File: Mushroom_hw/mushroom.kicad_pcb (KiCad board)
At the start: 2 copper layers, 49.2 x 83.8 mm, 129 parts, among them Q1 LED_RGB_WS2812B, Q2 LED_RGB, Q3 LED_RGB_WS2812B, Q4 LED_RGB, Q5 LED_RGB, Q6 LED_RGB_WS2812B, SW1 SWITCH_H

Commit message: + Component placement done
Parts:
- removed B1, B2, B3: BAT, BAT_AA
- removed C29, C30, C31: 0.1u, CAP_0603
- removed D1, D2, D3: SS14, DIODE_SMA_DO214AC
- removed DA3, DA4: TPS61042, DRB8
- removed F10, F11, F12, F13, F14, F15, F16, F17, F18, F19, F2, F20, F3, F4, F5, F6, F7, F8, F9: FUSE0R, SMD0603_FUSE
- removed L3: 6.8uH, IND_1210
- removed R10, R9: 390k, RES_0603
- removed R11, R16: 10k, RES_0603
- removed R12, R17: 13R, RES_0603
- removed R13, R18: 120k, RES_0603
- removed R14: 56k, RES_0603
- removed R15: 100k, RES_0603
- removed R19, R20, R21: 51R, RES_0603
- removed TP3: TESTPOINT, TESTPOINT_1MM
- removed XL14, XL16, XL17, XL18, XL20, XL21, XL22, XL24: CONN_3, SIL-3
- removed XL15, XL19, XL23: CONN_1, SIL1_ROUND_1MM8
- added BLN1: BALUN868JOHANSON, Radio:BALUN_JOHANSON868, F.Cu at (219.6, 130.0)
- added HOLE5: HOLE_METALLED, PCB:Hole2d4_out4d5mm, F.Cu at (249.0, 194.0)
- added HOLE6: HOLE_METALLED, PCB:Hole2d4_out4d5mm, F.Cu at (249.0, 124.0)
- added Logo1: Logo, Pictures:Ostranna_12d7_10d1, F.Cu at (239.0, 121.0)
- added RP3: REFPOINT, PCB:REF_POINT_1MM, B.Cu at (210.8, 195.2)
- added RP4: REFPOINT, PCB:REF_POINT_1MM, B.Cu at (250.2, 113.8)
- added SW2: BUTTON, BtnsSwitches:BTN_6x6_4x4, B.Cu at (243.0, 191.5)
- added SW3: BUTTON, BtnsSwitches:BTN_6x6_4x4, B.Cu at (221.5, 191.5)
- added SW4: BUTTON, BtnsSwitches:BTN_6x6_4x4, B.Cu at (232.0, 191.5)
- ANT1: value ANT_PCB_NOCNTR -> ANT_PCB_MONO; footprint ANT_FOLDED_DIPOLE2 -> Radio:ANT_868_ARMLETG
- C1, C20: value 0.1u -> 10u; footprint CAP_0603 -> Capacitors:CAP_0603
- C10: value 1u -> 10u; footprint CAP_0603 -> Capacitors:CAP_0603
- C11: value 10u -> 10n; footprint CAP_0805 -> Capacitors:CAP_0603
- C12, C23, C5, C7, C9: footprint CAP_0603 -> Capacitors:CAP_0603
- C13: value 10u -> 1u; footprint CAP_0805 -> Capacitors:CAP_0603
- C14: value 0.1u -> 220pF; footprint CAP_0603 -> Capacitors:CAP_0603
- C15, C21, C28, C3, C8: value 10u -> 0.1u; footprint CAP_0805 -> Capacitors:CAP_0603
- C16: footprint CAP_0805 -> Capacitors:CAP_0603
- C17: value 10pF -> 18pF; footprint CAP_0603 -> Capacitors:CAP_0603
- C18: value 10pF -> 10u; footprint CAP_0603 -> Capacitors:CAP_0603
- C19: value 0.1u -> 18pF; footprint CAP_0603 -> Capacitors:CAP_0603
- C2: value 10u -> 220pF; footprint CAP_0805 -> Capacitors:CAP_0603
- C22, C25, C27: value 220pF -> 0.1u; footprint CAP_0603 -> Capacitors:CAP_0603
- C24, C26: value 0.1u -> *; footprint CAP_0603 -> Capacitors:CAP_0402
- C4: value 0.1u -> 10n; footprint CAP_0603 -> Capacitors:CAP_0603
- C6: value 0.1u -> 3.3pF; footprint CAP_0603 -> Capacitors:CAP_0603
- DA1: value TPS61042 -> NCP583SQ; footprint DRB8 -> SOT:SC82AB
- DA2: value NCP583SQ -> MC74VHC1; footprint SC82AB -> SOT:SOT23-5
- DD1: value STM32L151CXTX -> STM32L151CxTx; footprint LQFP48 -> LQFP_TQFP:LQFP48
- DD2: value CC2500 -> CC1101; footprint QFN20 -> QFN_DFN:QFN20
- F1: value FUSE0R -> Fuse0R; footprint SMD0603_FUSE -> Resistors:RES_0603_FUSE
- HOLE1, HOLE2, HOLE3, HOLE4: footprint Hole3_5_out6mm -> PCB:Hole2d4_out4d5mm
- L1: value 6.8uH -> BLM15AG102SN1; footprint IND_1210 -> Inductors:IND_0402
- L2: value 6.8uH -> *; footprint IND_1210 -> Inductors:IND_0402
- Q1: value LED_RGB_WS2812B -> 2N7002; footprint LED_WS2812B -> SOT:SOT23-3
- Q2: value LED_RGB -> IRLML9303; footprint LED_HH5050_RGB -> SOT:SOT23-3
- Q3: value LED_RGB_WS2812B -> ALS-PT19-315C; footprint LED_WS2812B -> Resistors:RES_0603
- Q4, Q5: value LED_RGB -> LED_RGB_WS2812B; footprint LED_HH5050_RGB -> LEDs:LED_WS2812B
- Q6: footprint LED_WS2812B -> LEDs:LED_WS2812B
- R1, R2: value 4K7 -> 100k; footprint RES_0603 -> Resistors:RES_0603
- R3: footprint RES_0603 -> Resistors:RES_0603
- R4: value 150 -> 100k; footprint RES_0603 -> Resistors:RES_0603
- R5: value 10k -> 20k; footprint RES_0603 -> Resistors:RES_0603
- R6: value 13R -> 56k; footprint RES_0603 -> Resistors:RES_0603
- R7: value 120k -> 10k; footprint RES_0603 -> Resistors:RES_0603
- R8: value 100k -> 10k; footprint RES_0603 -> Resistors:RES_0603
- RP1, RP2: footprint REF_POINT_1MM -> PCB:REF_POINT_1MM
- SW1: value SWITCH_H -> SWITCH; footprint SWITCH_SS9 -> BtnsSwitches:SW_SS-1P2T
- TP1, TP2: footprint TESTPOINT_1MM -> PCB:TESTPOINT_1MM
- XL1: value CONN_3 -> CONN_6; footprint SIL-3 -> Connectors:PLS-6; moved to B.Cu
- XL10, XL12, XL6, XL8: footprint SIL-3 -> Connectors:PLS-3
- XL11, XL7: footprint SIL1_ROUND_1MM8 -> Connectors:SIL1_ROUND_1MM8
- XL13, XL5, XL9: value CONN_3 -> CONN_1; footprint SIL-3 -> Connectors:SIL1_ROUND_1MM8
- XL2: value ST_SWD -> CONN_1; footprint SIL-4 -> Connectors:PLS-1Rnd
- XL3: value CONN_4 -> CONN_2; footprint SIL-4 -> Connectors:W02_Pitch_2d54; moved to B.Cu
- XL4: value CONN_4 -> CONN_3; footprint SIL-4 -> Connectors:PLS-3
- XTAL1: footprint CRYSTAL_03225C4 -> Quartz:03225C4
- moved RP1 103.6 mm to (250.2, 113.8)
- moved XL2 86.2 mm to (250.5, 128.5)
- moved C9 71.9 mm to (223.8, 134.7)
- moved C6 71.0 mm to (222.5, 130.2), turned to 0 degrees
- moved C4 64.7 mm to (217.5, 129.5)
- moved C12 62.2 mm to (219.5, 139.9)
- moved RP2 59.6 mm to (210.8, 195.2)
- moved C21 56.6 mm to (221.1, 139.9), turned to 90 degrees
- moved L2 54.3 mm to (219.0, 127.8), turned to 270 degrees
- moved HOLE2 54.1 mm to (220.0, 165.0)
- moved DA2 48.9 mm to (211.8, 155.1), turned to 0 degrees
- moved R2 48.8 mm to (212.9, 165.2)
- moved C14 48.6 mm to (214.0, 135.5)
- moved C28 48.6 mm to (233.4, 157.0)
- moved HOLE4 47.4 mm to (207.0, 124.0)
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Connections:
- ANT1 pad 1: /Ant -> /ANT2
- C1 pad 1: +BATT -> GND
- C1 pad 2: GND -> +3.3V
- C10 pad 1: +3.3V -> +BATT
- C11 pad 1: /RED_P -> +3.3V
- C12 pad 1: +3.3V -> VCC
- C14 pad 1: +BATT -> VCC
- C15 pad 1: +BATT -> +3.3V
- C16 pad 1: /GREEN_P -> +3.3V
- C18 pad 1: N-000005 -> GND
- C18 pad 2: GND -> PwrUnst
- C19 pad 1: N-0000010 -> Net-(C19-Pad1)
- C2 pad 1: +BATT -> VCC
- C20 pad 1: +BATT -> GND
- C20 pad 2: GND -> PwrUnst
- C21 pad 1: +BATT -> GND
- C21 pad 2: GND -> Net-(C21-Pad2)
- C22 pad 1: +3.3V -> PwrUnst
- C23 pad 1: +3.3V -> /ADC_LUM
- C24 pad 1: +3.3V -> /ANT1
- C25 pad 1: +3.3V -> PwrUnst
- C26 pad 1: +3.3V -> /ANT2
- C27 pad 1: +3.3V -> PwrUnst
- C28 pad 1: /BLUE_P -> PwrUnst
- C4 pad 1: +3.3V -> VCC
- C6 pad 1: +BATT -> VCC
- C7 pad 1: +3.3V -> +BATT
- C8 pad 1: +BATT -> +3.3V
- C9 pad 1: +3.3V -> VCC
- DA1 pad 1: /RED_N -> +BATT
- DA1 pad 2: N-000007 -> GND
- DA1 pad 3: +BATT -> +3.3V
- DA1 pad 4: N-000006 -> +BATT
- DA2 pad 1: +BATT -> Net-(DA2-Pad1)
- DA2 pad 2: GND -> /WS_CTRL
- DA2 pad 3: +3.3V -> GND
- DA2 pad 4: +BATT -> /DIN0
- DD1 pad 10: N-000008 -> /BTN1
- DD1 pad 11: /CC_GDO2 -> /BTN2
- DD1 pad 12: /CC_CS -> /ADC_BATTERY
- DD1 pad 14: /BRIGHTNESS -> /CC_CS
- DD1 pad 18: /RED_PWM -> /ADC_LUM
- DD1 pad 19: /GREEN_PWM -> /MEAS_LUM
- DD1 pad 21: N-0000032 -> (no net)
- DD1 pad 22: N-0000033 -> (no net)
- DD1 pad 25: N-0000031 -> (no net)
- DD1 pad 27: (no net) -> /PWR_EN
- DD1 pad 28: /DIN0 -> /WS_CTRL
- DD1 pad 29: (no net) -> /BTN3
- DD1 pad 41: /BLUE_PWM -> (no net)
- DD1 pad 43: /PeriphPwr -> /NO_RADIO
- DD1 pad 45: /P_SCL -> (no net)
- DD1 pad 46: /P_SDA -> (no net)
- DD2 pad 10: N-000005 -> Net-(C19-Pad1)
- DD2 pad 11: +3.3V -> VCC
- DD2 pad 12: /Ant -> /RF1
- DD2 pad 13: /Ant -> /RF2
- DD2 pad 14: +3.3V -> VCC
- DD2 pad 15: +3.3V -> VCC
- DD2 pad 17: N-0000013 -> Net-(DD2-Pad17)
- DD2 pad 18: +3.3V -> VCC
- DD2 pad 3: /CC_GDO2 -> (no net)
- DD2 pad 4: +3.3V -> VCC
- DD2 pad 5: N-0000010 -> Net-(C21-Pad2)
- DD2 pad 9: +3.3V -> VCC
- F1 pad 1: GND -> +3.3V
- F1 pad 2: N-0000070 -> /NO_RADIO
- L1 pad 1: N-0000017 -> VCC
- L1 pad 2: +BATT -> +3.3V
- L2 pad 1: N-0000016 -> /ANT2
- L2 pad 2: +BATT -> /ANT1
- Q1 pad 1: +BATT -> /PWR_EN
- Q1 pad 2: N-0000059 -> GND
- Q1 pad 3: GND -> Net-(Q1-Pad3)
- Q3 pad 1: +BATT -> +3.3V
- Q3 pad 2: N-0000058 -> /ADC_LUM
- Q6 pad 1: +BATT -> PwrUnst
- Q6 pad 4: N-0000058 -> Net-(Q5-Pad2)
- R1 pad 1: /P_SCL -> PwrUnst
- R1 pad 2: /PeriphPwr -> /ADC_BATTERY
- R2 pad 1: /P_SDA -> /ADC_BATTERY
- R2 pad 2: /PeriphPwr -> GND
- R3 pad 1: /RED_PWM -> /PWR_EN
- R4 pad 1: /PeriphPwr1 -> +BATT
- R4 pad 2: /PeriphPwr -> Net-(Q1-Pad3)
- R5 pad 1: N-000007 -> /CC_CS
- R5 pad 2: N-000006 -> VCC
- R6 pad 1: N-000007 -> Net-(DD2-Pad17)
- R7 pad 1: N-000006 -> Net-(DA2-Pad1)
- R7 pad 2: /BRIGHTNESS -> PwrUnst
- R8 pad 1: /GREEN_PWM -> /ADC_LUM
- R8 pad 2: GND -> /MEAS_LUM
- SW1 pad 1: /BAT_IN -> +BATT
- SW1 pad 2: +BATT -> /BAT_IN
- XL1 pad 1: GND -> +3.3V
- XL1 pad 2: /UART_TX -> /SWCLK
- XL1 pad 3: /UART_RX -> GND
- XL10 pad 1: /DIN1 -> /DIN3
- XL10 pad 2: +BATT -> PwrUnst
- XL10 pad 3: /DIN2 -> /DIN4
- XL11 pad 1: N-0000071 -> GND
- XL12 pad 1: N-0000022 -> /DIN4
- XL12 pad 2: N-0000021 -> PwrUnst
- XL12 pad 3: N-0000020 -> (no net)
- XL13 pad 1: N-0000022 -> GND
- XL2 pad 1: +3.3V -> GND
- XL3 pad 1: /PeriphPwr1 -> /BAT_IN
- XL3 pad 2: /P_SCL -> GND
- XL4 pad 1: N-0000032 -> /DIN0
- XL4 pad 2: N-0000033 -> PwrUnst
- XL4 pad 3: N-0000031 -> /DIN1
- XL5 pad 1: /RED_P -> GND
- XL6 pad 1: /DIN0 -> /DIN1
- XL6 pad 2: +BATT -> PwrUnst
- XL6 pad 3: /DIN1 -> /DIN2
- XL7 pad 1: N-0000070 -> GND
- XL8 pad 1: N-0000028 -> /DIN2
- XL8 pad 2: N-0000027 -> PwrUnst
- XL8 pad 3: N-0000026 -> /DIN3
- XL9 pad 1: N-0000028 -> GND
- XTAL1 pad 2: N-000005 -> Net-(C19-Pad1)
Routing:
- net GND: track 812.5 -> 0.00 mm, vias 151 -> 0
- net +3.3V: track 177.8 -> 0.00 mm, vias 10 -> 0
- net +BATT: track 159.2 -> 0.00 mm, vias 2 -> 0
- net /BLUE_P: track 78.3 -> 0.00 mm, vias 1 -> 0
- net /BRIGHTNESS: track 73.8 -> 0.00 mm, vias 4 -> 0
- net /BLUE_PWM: track 68.9 -> 0.00 mm, vias 2 -> 0
- net /GREEN_P: track 62.2 -> 0.00 mm, vias 1 -> 0
- net /GREEN_PWM: track 61.7 -> 0.00 mm, vias 2 -> 0
- net /RED_N: track 60.8 -> 0.00 mm, vias 3 -> 0
- net /RED_PWM: track 58.2 -> 0.00 mm, vias 2 -> 0
- net /BLUE_N: track 58.1 -> 0.00 mm, vias 4 -> 0
- net /CC_GDO2: track 58.0 -> 0.00 mm
- net /DIN0: track 57.0 -> 0.00 mm, vias 1 -> 0
- net /CC_MOSI: track 55.4 -> 0.00 mm
- net /CC_MISO: track 55.0 -> 0.00 mm
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- removed copper zone on B.Cu, net GND
- removed copper zone on F.Cu, net GND
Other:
- board size 49.2 x 83.8 mm -> 48 x 85 mm

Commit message: HW2 sent to production
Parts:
- moved XL10 11.5 mm to (236.6, 172.8)
- moved XL12 11.4 mm to (225.2, 172.8)
- moved R5 10.2 mm to (224.0, 139.8), turned to 270 degrees
- moved TP2 5.68 mm to (221.5, 142.4)
- moved L1 2.40 mm to (213.6, 138.6), turned to 180 degrees
- moved C17 1.02 mm to (226.4, 137.6)
- moved XTAL1 0.41 mm to (226.4, 134.4)
- moved C9 0.30 mm to (223.8, 134.4)
- moved C19 0.22 mm to (226.4, 131.2)
- moved C12 0.14 mm to (219.6, 139.8)
- moved C21 0.14 mm to (221.2, 139.8)
- moved C4 0.14 mm to (217.4, 129.4)
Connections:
- DD1 pad 11: /BTN2 -> /BTN3
- DD1 pad 29: /BTN3 -> /BTN2
- SW3 pad 1: /BTN2 -> /BTN3
- SW4 pad 1: /BTN3 -> /BTN2
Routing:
- net GND: track 0.00 -> 1013.3 mm, vias 0 -> 209
- net PwrUnst: track 0.00 -> 131.5 mm, vias 0 -> 2
- net +3.3V: track 0.00 -> 121.7 mm, vias 0 -> 6
- net VCC: track 0.00 -> 56.5 mm, vias 0 -> 6
- net /BTN2: track 0.00 -> 46.0 mm, vias 0 -> 1
- net /BTN1: track 0.00 -> 42.3 mm, vias 0 -> 1
- net /CC_CS: track 0.00 -> 38.7 mm, vias 0 -> 2
- net /CC_GDO0: track 0.00 -> 36.9 mm, vias 0 -> 2
- net /CC_MOSI: track 0.00 -> 35.7 mm, vias 0 -> 2
- net /CC_MISO: track 0.00 -> 34.8 mm, vias 0 -> 2
- net /CC_SCK: track 0.00 -> 34.7 mm, vias 0 -> 2
- net /UART_RX: track 0.00 -> 29.8 mm, vias 0 -> 1
- net /BTN3: track 0.00 -> 29.7 mm, vias 0 -> 1
- net /UART_TX: track 0.00 -> 27.8 mm, vias 0 -> 1
- net +BATT: track 0.00 -> 26.0 mm
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- added copper zone on B.Cu, net GND
- added copper zone on F.Cu, net GND
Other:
- net class Default: via_dia 0.9 -> 0.7; via_drill 0.4 -> 0.3
- net class Wide: via_dia 0.9 -> 0.7; via_drill 0.4 -> 0.3
- rule via_min_drill: 0.4 -> 0.2
- rule via_min_size: 0.889 -> 0.6
- board text added: "+"
- board text added: "-"
- board text added: "3V3 Power Supply"
- board text added: "Btn1"
- board text added: "Btn2"
- board text added: "Btn3"
- board text added: "Crystal Mushroom v2"
- board text added: "GND"
- board text added: "In"
- board text added: "LED A"
- board text added: "LED B"
- board text added: "LED C"
- board text added: "LED Power Control"
- board text added: "LED1"
- board text added: "LED2"
- board text added: "LED3"
- board text added: "LED4"
- board text added: "LED5"
- board text added: "Level Shifter"
- board text added: "Light detector"
- board text added: "MCU"
- board text added: "Ostranna"
- board text added: "Out"
- board text added: "Radio"
- board text added: "Solder if radio not mounted"

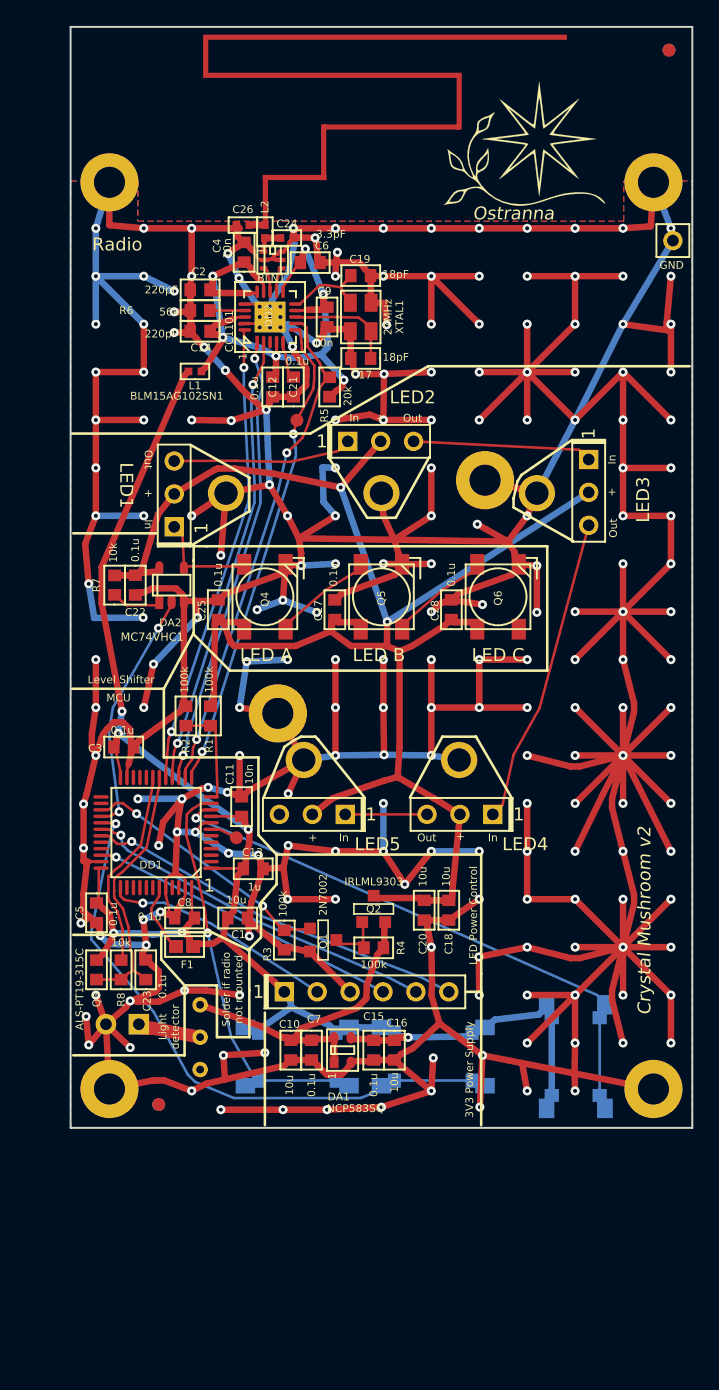
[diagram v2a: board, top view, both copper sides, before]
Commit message: + IFA antenna
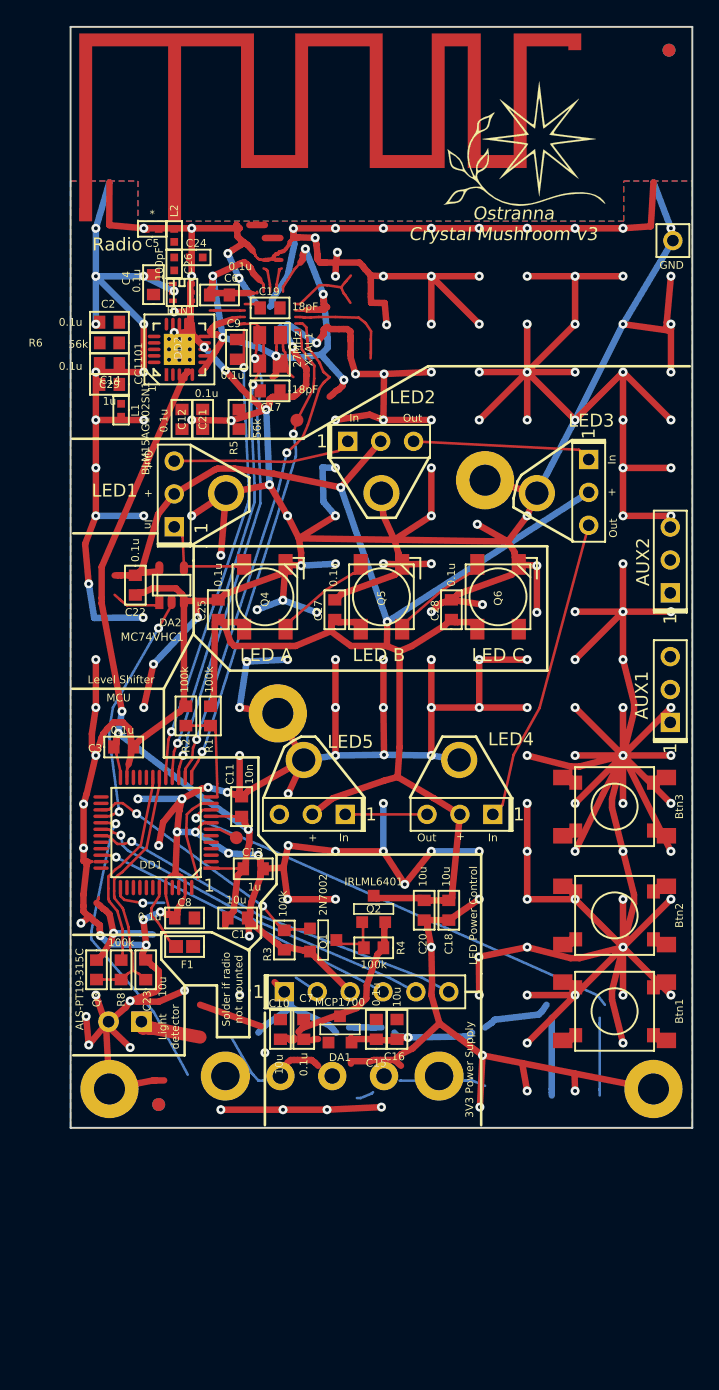
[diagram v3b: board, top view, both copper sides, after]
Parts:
- removed HOLE4, HOLE6: HOLE_METALLED, PCB:Hole2d4_out4d5mm
- removed R7: 10k, Resistors:RES_0603
- added C29: 1u, Capacitors:CAP_0603, F.Cu at (207.0, 139.6)
- added XL14: CONN_3, Connectors:PLS-3, F.Cu at (250.3, 165.7)
- added XL15: CONN_3, Connectors:PLS-3, F.Cu at (250.3, 155.7)
- ANT1: value ANT_PCB_MONO -> AntIFAMushroom; footprint Radio:ANT_868_ARMLETG -> Radio:ANT_IFA_MUSHROOM
- C14, C2: value 220pF -> 0.1u
- C23: value 0.1u -> 10u
- C26: value * -> 100pF
- C4, C9: value 10n -> 0.1u
- C5: value 0.1u -> *; footprint Capacitors:CAP_0603 -> Capacitors:CAP_0402
- C6: value 3.3pF -> 0.1u
- DA1: value NCP583SQ -> MCP1700; footprint SOT:SC82AB -> SOT:SOT23-3
- DD1: value STM32L151CxTx -> STM32F030C8Tx
- Q2: value IRLML9303 -> IRLML6401
- R5: value 20k -> 56k
- R8: value 10k -> 100k
- SW1: value SWITCH -> SS-9; footprint BtnsSwitches:SW_SS-1P2T -> BtnsSwitches:SW_SS9
- SW2, SW3, SW4: moved to F.Cu
- moved C5 53.0 mm to (210.3, 127.6), turned to 180 degrees
- moved SW3 31.2 mm to (246.0, 172.2), turned to 180 degrees
- moved SW4 17.7 mm to (246.0, 180.6)
- moved ANT1 16.0 mm to (212.0, 127.0)
- moved SW1 10.6 mm to (224.2, 193.0), turned to 0 degrees
- moved BLN1 7.43 mm to (212.6, 132.5)
- moved C12 7.43 mm to (212.6, 142.3)
- moved C14 7.43 mm to (207.0, 138.0)
- moved C17 7.43 mm to (219.4, 140.1)
- moved C19 7.43 mm to (219.4, 133.7)
- moved C2 7.43 mm to (207.0, 134.8)
- moved C21 7.43 mm to (214.2, 142.3)
- moved C4 7.43 mm to (210.4, 131.9)
- moved C6 7.43 mm to (215.5, 132.7)
- moved C9 7.43 mm to (216.8, 136.9)
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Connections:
- BLN1 pad 1: /ANT1 -> Net-(BLN1-Pad1)
- C26 pad 1: /ANT2 -> /ANT1
- C26 pad 2: GND -> Net-(BLN1-Pad1)
- C5 pad 1: +3.3V -> /ANT2
- DA1 pad 1: +BATT -> GND
- DA1 pad 2: GND -> +3.3V
- DA1 pad 3: +3.3V -> +BATT
- DA2 pad 1: Net-(DA2-Pad1) -> GND
- DD1 pad 2: (no net) -> Net-(DD1-Pad2)
- DD1 pad 20: (no net) -> Net-(DD1-Pad20)
- DD1 pad 21: (no net) -> Net-(DD1-Pad21)
- DD1 pad 22: (no net) -> Net-(DD1-Pad22)
- DD1 pad 25: (no net) -> Net-(DD1-Pad25)
- DD1 pad 26: (no net) -> Net-(DD1-Pad26)
- DD1 pad 3: (no net) -> Net-(DD1-Pad3)
- DD1 pad 32: (no net) -> Net-(DD1-Pad32)
- DD1 pad 33: (no net) -> Net-(DD1-Pad33)
- DD1 pad 35: GND -> Net-(DD1-Pad35)
- DD1 pad 36: +3.3V -> Net-(DD1-Pad36)
- DD1 pad 38: (no net) -> Net-(DD1-Pad38)
- DD1 pad 39: (no net) -> Net-(DD1-Pad39)
- DD1 pad 4: (no net) -> Net-(DD1-Pad4)
- DD1 pad 40: (no net) -> /AUX1
- DD1 pad 41: (no net) -> /AUX2
- DD1 pad 42: (no net) -> Net-(DD1-Pad42)
- DD1 pad 45: (no net) -> Net-(DD1-Pad45)
- DD1 pad 46: (no net) -> Net-(DD1-Pad46)
- DD1 pad 5: (no net) -> Net-(DD1-Pad5)
- DD1 pad 6: (no net) -> Net-(DD1-Pad6)
- DD2 pad 3: (no net) -> Net-(DD2-Pad3)
- Q6 pad 2: (no net) -> Net-(Q6-Pad2)
- SW1 pad 3: (no net) -> Net-(SW1-Pad3)
- XL12 pad 3: (no net) -> Net-(XL12-Pad3)
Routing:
- net GND: track 1013.3 -> 949.2 mm, vias 209 -> 199
- net /BTN3: track 29.7 -> 7.26 mm, vias 1 -> 0
- net +3.3V: track 121.7 -> 103.4 mm, vias 6 -> 5
- net /BTN2: track 46.0 -> 31.2 mm
- net /SWCLK: track 17.9 -> 6.15 mm
- net Net-(DA2-Pad1): track 3.87 -> 0.00 mm
- net Net-(C19-Pad1): track 6.72 -> 10.0 mm
- net +BATT: track 26.0 -> 23.1 mm
- net /ANT1: track 2.25 -> 1.20 mm
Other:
- net class Default: trace_width 0.2 -> 0.25
- board text added: "AUX1"
- board text added: "AUX2"
- board text added: "Crystal Mushroom v3"
- board text removed: "Crystal Mushroom v2"

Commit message: + PCB v3
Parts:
- moved TP2 5.83 mm to (215.7, 141.5)
- moved R5 1.20 mm to (218.2, 142.4)
- moved C24 1.20 mm to (213.7, 128.6)
- moved TP1 0.88 mm to (216.6, 175.5)
- moved C4 0.14 mm to (210.5, 132.0)
- moved BLN1 0.09 mm to (212.7, 132.5)
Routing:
- net +3.3V: track 103.4 -> 167.3 mm, vias 5 -> 6
- net /AUX2: track 0.00 -> 51.6 mm, vias 0 -> 1
- net /AUX1: track 0.00 -> 46.9 mm, vias 0 -> 1
- net /BTN3: track 7.26 -> 37.2 mm, vias 0 -> 2
- net GND: track 949.2 -> 919.9 mm, vias 199 -> 175
- net PwrUnst: track 131.5 -> 116.2 mm
- net /BAT_IN: track 4.92 -> 18.5 mm
- net /SWCLK: track 6.15 -> 17.8 mm
- net /BTN2: track 31.2 -> 42.2 mm, vias 1 -> 2
- net +BATT: track 23.1 -> 19.5 mm
- net /CC_GDO0: track 36.9 -> 33.4 mm
- net Net-(C19-Pad1): track 10.0 -> 6.67 mm
- net /CC_MOSI: track 35.7 -> 32.9 mm
- net /CC_MISO: track 34.8 -> 32.3 mm
- net /CC_SCK: track 34.7 -> 32.2 mm
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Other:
- board text added: "E"

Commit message: + PCB v4
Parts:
- removed C5: *, Capacitors:CAP_0402
- C24: value * -> 3pF
- L2: value * -> 3.3nH
- moved XL3 26.0 mm to (233.9, 193.0)
- moved C16 9.30 mm to (238.0, 186.4)
- moved C15 9.01 mm to (236.1, 186.4)
- moved C7 9.01 mm to (230.5, 186.4)
- moved DA1 9.01 mm to (233.3, 186.4)
- moved C10 8.92 mm to (228.6, 186.4)
- moved XL1 7.32 mm to (213.2, 187.0)
- moved RP2 7.27 mm to (207.0, 189.0)
- moved RP3 7.27 mm to (207.0, 189.0)
- moved SW1 4.70 mm to (219.5, 193.0), turned to 180 degrees
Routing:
- net GND: track 919.9 -> 940.5 mm, vias 175 -> 172
- net /UART_RX: track 29.7 -> 23.6 mm
- net /UART_TX: track 27.9 -> 21.9 mm
- net /SWDIO: track 24.3 -> 18.5 mm
- net /SWCLK: track 17.8 -> 12.1 mm
- net +3.3V: track 167.3 -> 170.1 mm
- net VCC: track 56.2 -> 58.1 mm
- net /BAT_IN: track 18.5 -> 16.7 mm
- net /ANT2: track 2.30 -> 1.10 mm
- net +BATT: track 19.5 -> 18.7 mm
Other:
- board text added: "Crystal Mushroom v4"
- board text removed: "Crystal Mushroom v3"

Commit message: + Colindo Board job
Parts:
- added C5: *, Capacitors:CAP_0402, F.Cu at (210.3, 127.6)
- C24: value 3pF -> *
- L2: value 3.3nH -> *
- moved XL3 26.0 mm to (208.2, 188.8)
- moved C16 9.30 mm to (229.2, 189.4)
- moved C15 9.01 mm to (227.6, 189.4)
- moved C7 9.01 mm to (222.0, 189.4)
- moved DA1 9.01 mm to (224.8, 189.4)
- moved C10 8.92 mm to (220.2, 189.4)
- moved XL1 7.32 mm to (220.5, 186.5)
- moved RP2 7.27 mm to (210.8, 195.2)
- moved RP3 7.27 mm to (210.8, 195.2)
- moved SW1 4.70 mm to (224.2, 193.0), turned to 0 degrees
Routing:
- net GND: track 940.5 -> 919.9 mm, vias 172 -> 175
- net /UART_RX: track 23.6 -> 29.7 mm
- net /UART_TX: track 21.9 -> 27.9 mm
- net /SWDIO: track 18.5 -> 24.3 mm
- net /SWCLK: track 12.1 -> 17.8 mm
- net +3.3V: track 170.1 -> 167.3 mm
- net VCC: track 58.1 -> 56.2 mm
- net /BAT_IN: track 16.7 -> 18.5 mm
- net /ANT2: track 1.10 -> 2.30 mm
- net +BATT: track 18.7 -> 19.5 mm
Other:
- board text added: "Crystal Mushroom v3"
- board text removed: "Crystal Mushroom v4"

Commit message: +v4 without silks, but ready for production
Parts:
- moved XL3 26.0 mm to (233.9, 193.0)
- moved C16 9.30 mm to (238.0, 186.4)
- moved C15 9.01 mm to (236.1, 186.4)
- moved C7 9.01 mm to (230.5, 186.4)
- moved DA1 9.01 mm to (233.3, 186.4)
- moved C10 8.92 mm to (228.6, 186.4)
- moved XL1 7.32 mm to (213.2, 187.0)
- moved RP2 7.27 mm to (207.0, 189.0)
- moved RP3 7.27 mm to (207.0, 189.0)
- moved SW1 4.70 mm to (219.5, 193.0), turned to 180 degrees
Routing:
- net GND: track 919.9 -> 940.5 mm, vias 175 -> 172
- net /UART_RX: track 29.7 -> 23.6 mm
- net /UART_TX: track 27.9 -> 21.9 mm
- net /SWDIO: track 24.3 -> 18.5 mm
- net /SWCLK: track 17.8 -> 12.1 mm
- net +3.3V: track 167.3 -> 170.1 mm
- net VCC: track 56.2 -> 58.1 mm
- net /BAT_IN: track 18.5 -> 16.7 mm
- net +BATT: track 19.5 -> 18.7 mm
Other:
- board text added: "Crystal Mushroom v4"
- board text removed: "Crystal Mushroom v3"
